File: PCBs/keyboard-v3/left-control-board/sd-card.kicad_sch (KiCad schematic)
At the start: 12 parts, among them J105 MSD-1-A, U103 GL835

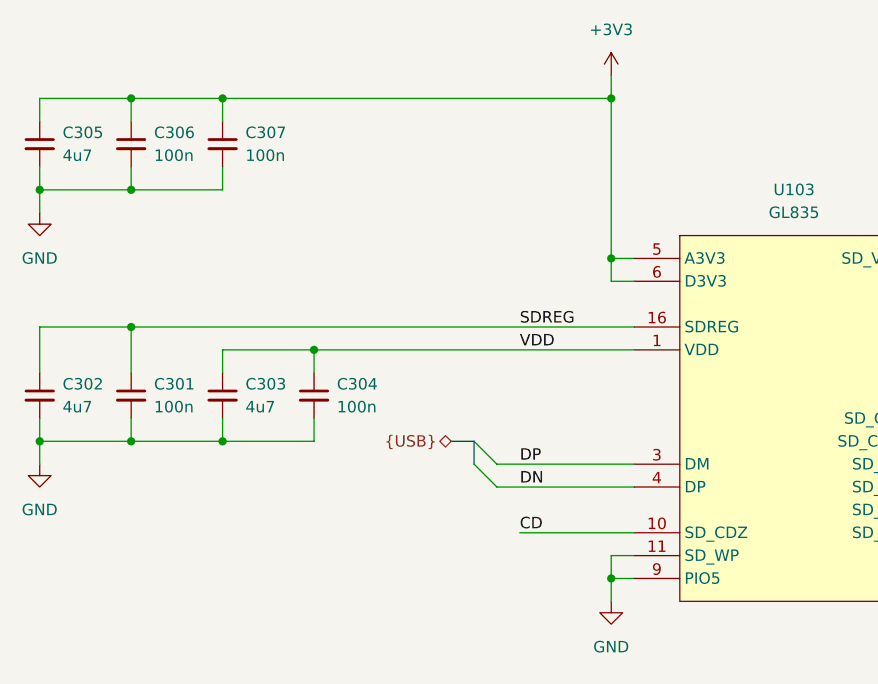
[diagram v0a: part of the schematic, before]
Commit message: Added power gate to AS5600 to reduce its sleep current
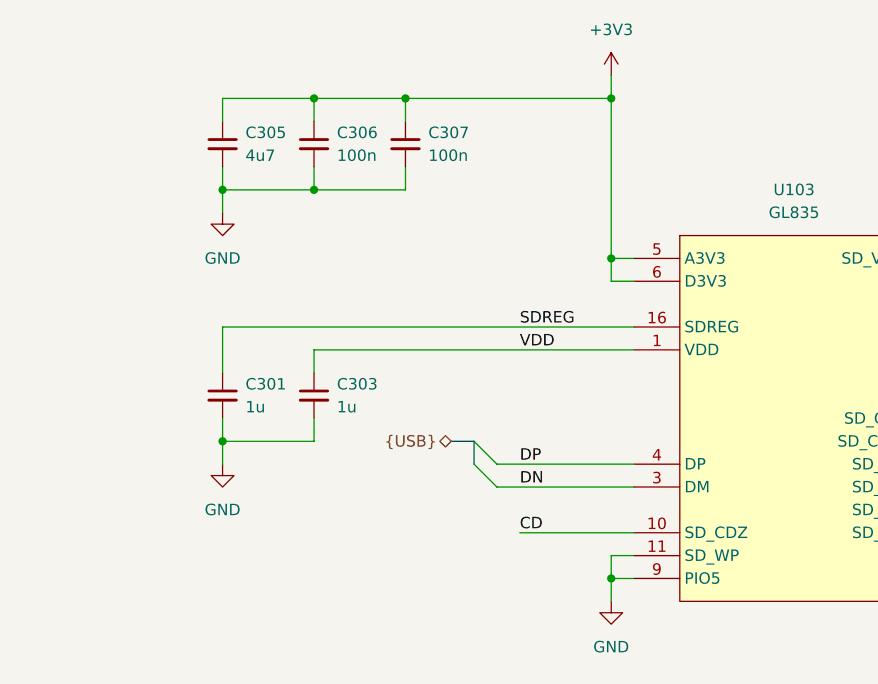
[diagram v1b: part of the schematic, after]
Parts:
- removed C302: 4u7, project_footprints:C_0402, symbol DEV:C_SMALL
- removed C304: 100n, project_footprints:C_0402, symbol DEV:C_SMALL
- C301: value 100n -> 1u
- C303: value 4u7 -> 1u
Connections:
- net DN: now also U103.3 (DM); no longer U103.4 (DP)
- net DP: now also U103.4 (DP); no longer U103.3 (DM)
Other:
- moved on the sheet: C303, C305, C306, C307

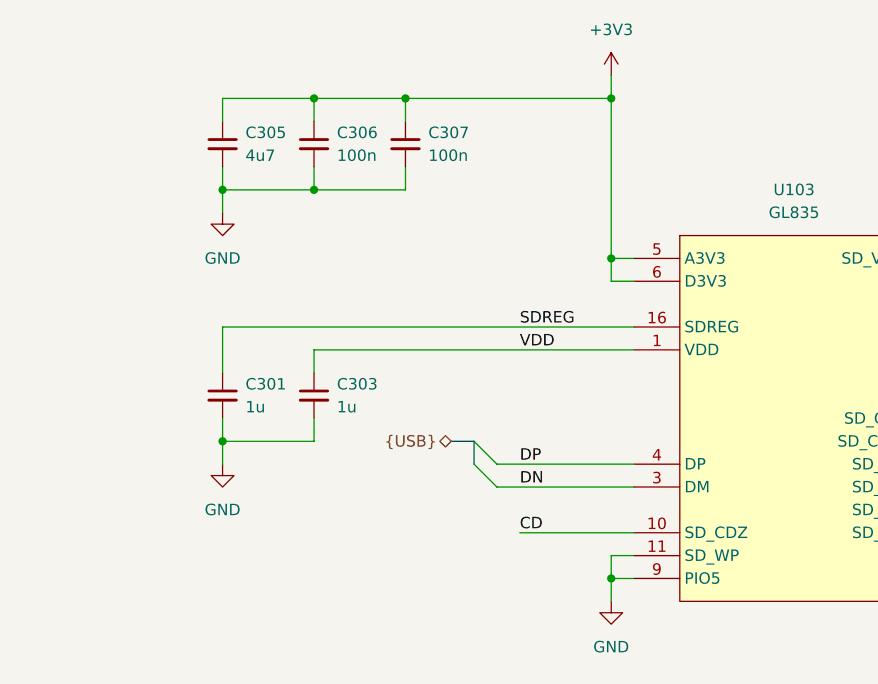
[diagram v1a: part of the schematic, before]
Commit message: Left knob board done
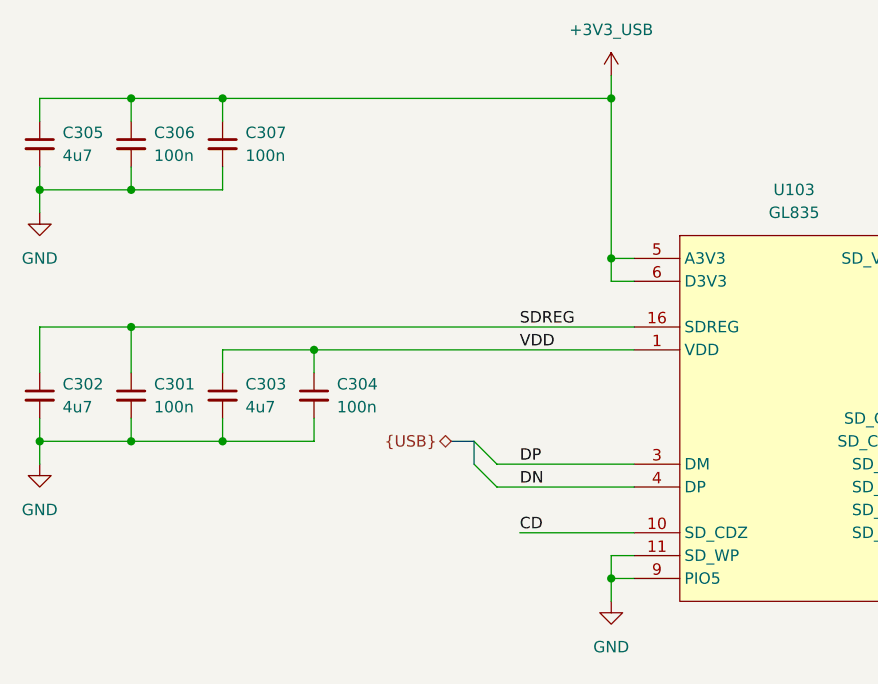
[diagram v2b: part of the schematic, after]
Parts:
- added C302: 4u7, project_footprints:C_0402, symbol DEV:C_SMALL
- added C304: 100n, project_footprints:C_0402, symbol DEV:C_SMALL
- C301: value 1u -> 100n
- C303: value 1u -> 4u7
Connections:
- net DN: now also U103.4 (DP); no longer U103.3 (DM)
- net DP: now also U103.3 (DM); no longer U103.4 (DP)
- net GND: now also C302.2, C304.2
- net SDREG: now also C302.1
- net VDD: now also C304.1
- net +3V3 renamed +3V3_USB
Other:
- moved on the sheet: C303, C305, C306, C307
